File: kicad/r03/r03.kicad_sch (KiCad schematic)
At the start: 0 parts

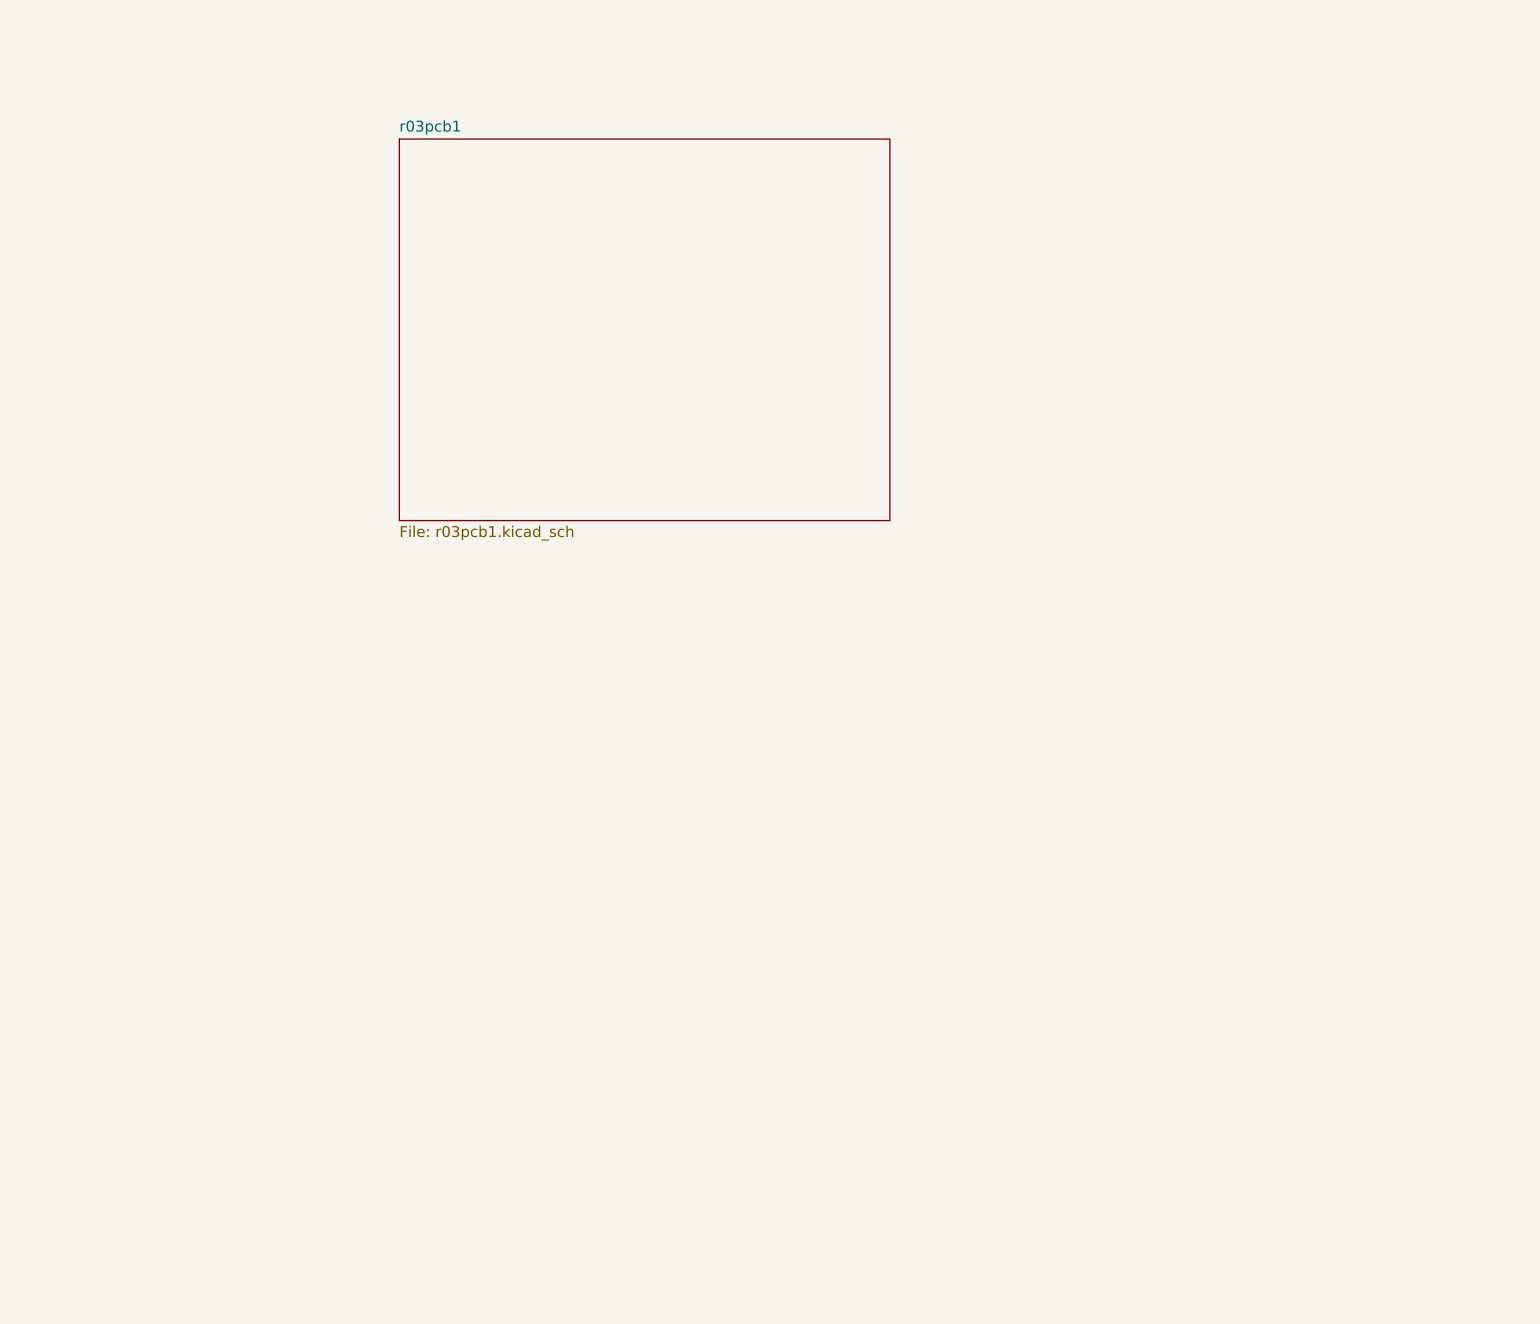
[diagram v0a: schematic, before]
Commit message: r03: started mcu pcb (pcb2), deleted r01
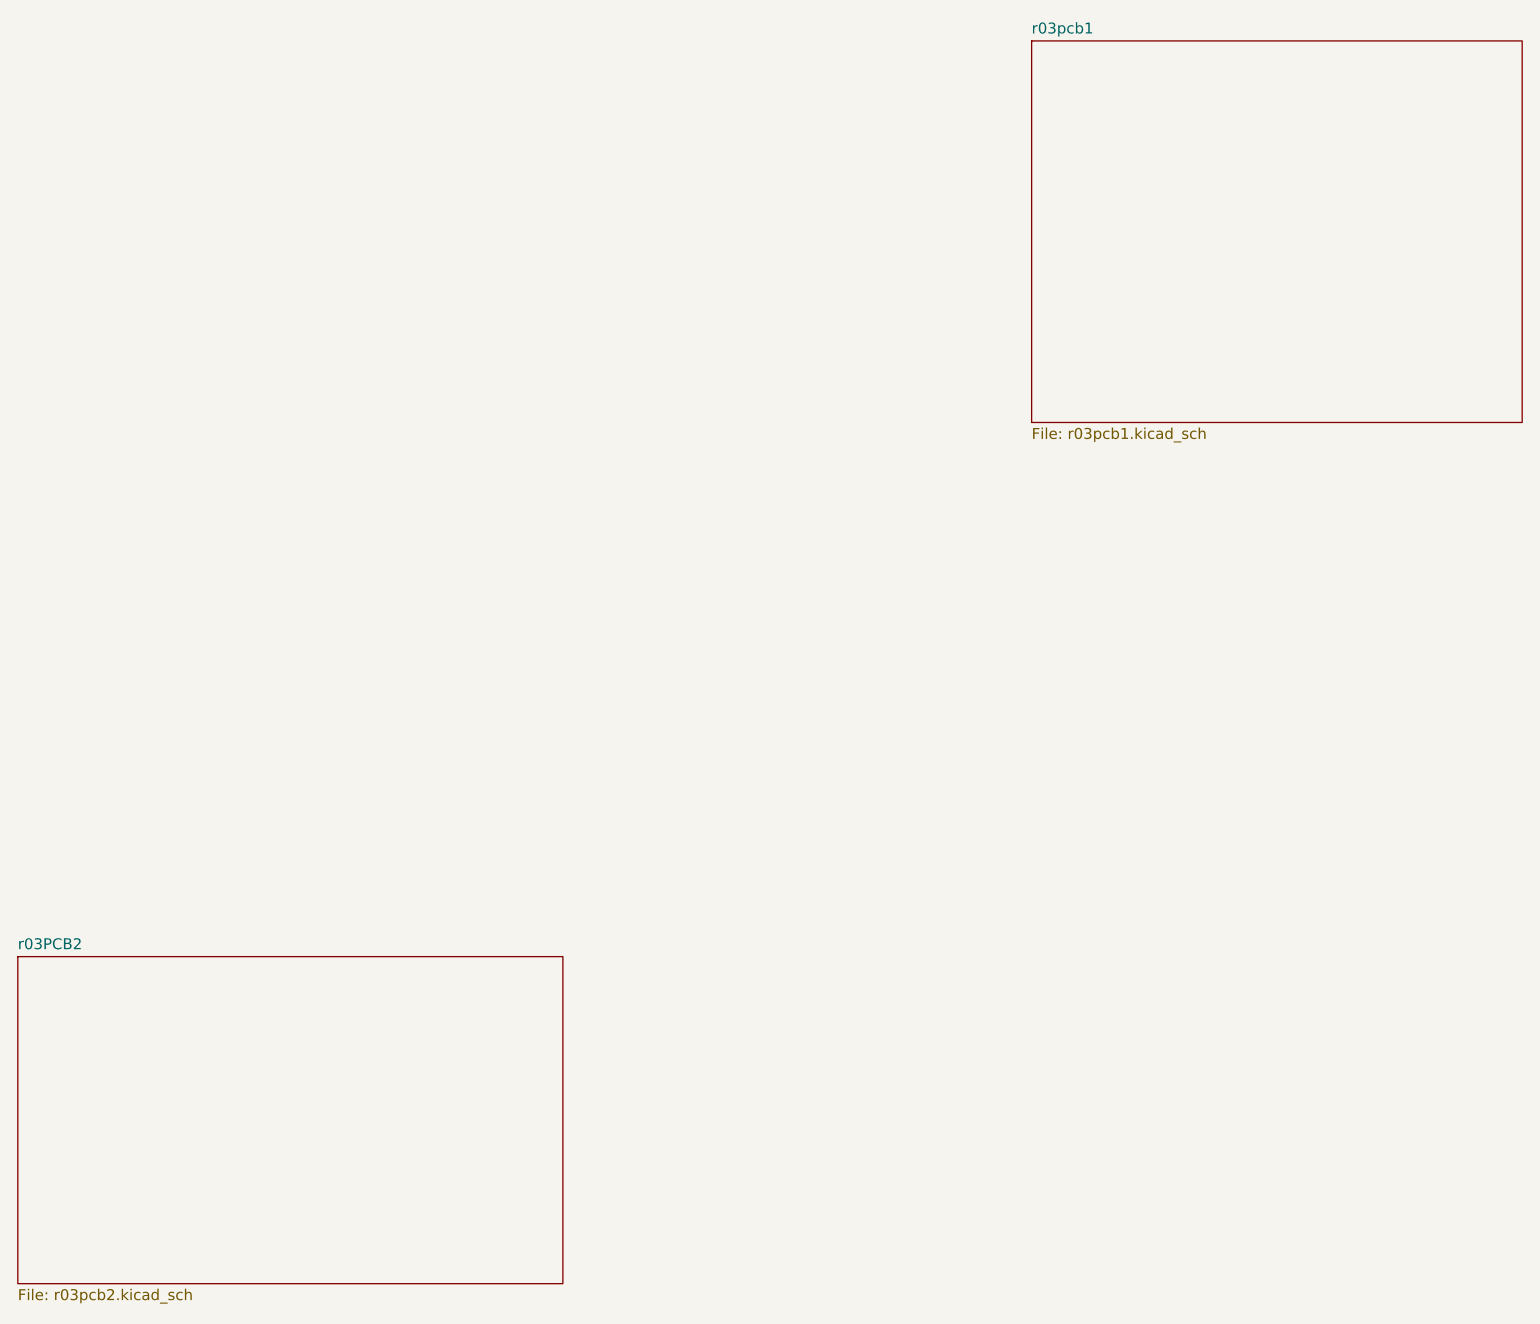
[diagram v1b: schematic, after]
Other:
- added sheet r03PCB2 (r03pcb2.kicad_sch)
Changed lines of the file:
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@@
     (company "MEgliDevelopment")
   )
-  (sheet (at 129.54 38.1) (size 57.15 44.45) (fields_autoplaced)
+  (sheet (at 85.09 133.35) (size 63.5 38.1) (fields_autoplaced)
     (stroke (width 0.1524) (type solid))
     (fill (color 0 0 0 0.0000))
-    (property "Sheetname" "r03pcb1" (at 129.54 37.3884 0)
+    (property "Sheetname" "r03PCB2" (at 85.09 132.6384 0)
       (effects (font (size 1.27 1.27)) (justify left bottom))
     )
-    (property "Sheetfile" "r03pcb1.kicad_sch" (at 129.54 83.1346 0)
+    (property "Sheetfile" "r03pcb2.kicad_sch" (at 85.09 172.0346 0)
       (effects (font (size 1.27 1.27)) (justify left top))
     )
-    (property "Field2" "" (at 129.54 38.1 0)
+    (property "Field2" "" (at 85.09 133.35 0)
       (effects (font (size 1.27 1.27)) hide)
     )
+    (instances
+      (project "r03"
+        (path "/c886117b-523f-45ec-8dd9-7a358aad202b" (page "3"))
+      )
+    )
+  )
+  (sheet (at 203.2 26.67) (size 57.15 44.45) (fields_autoplaced)
+    (stroke (width 0.1524) (type solid))
+    (fill (color 0 0 0 0.0000))
+    (property "Sheetname" "r03pcb1" (at 203.2 25.9584 0)
+      (effects (font (size 1.27 1.27)) (justify left bottom))
+    )
+    (property "Sheetfile" "r03pcb1.kicad_sch" (at 203.2 71.7046 0)
+      (effects (font (size 1.27 1.27)) (justify left top))
+    )
+    (property "Field2" "" (at 203.2 26.67 0)
+      (effects (font (size 1.27 1.27)) hide)
+    )
